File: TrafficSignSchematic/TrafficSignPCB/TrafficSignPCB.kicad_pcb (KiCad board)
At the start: 2 copper layers, 106.7 x 78.7 mm, 27 parts, among them J1 IDC connector, J2 3.96mm pitch 4-pin polarized 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, J3 Power In, U1 ATmega328P-PU, U2 SIM800L, Y1 16MHz

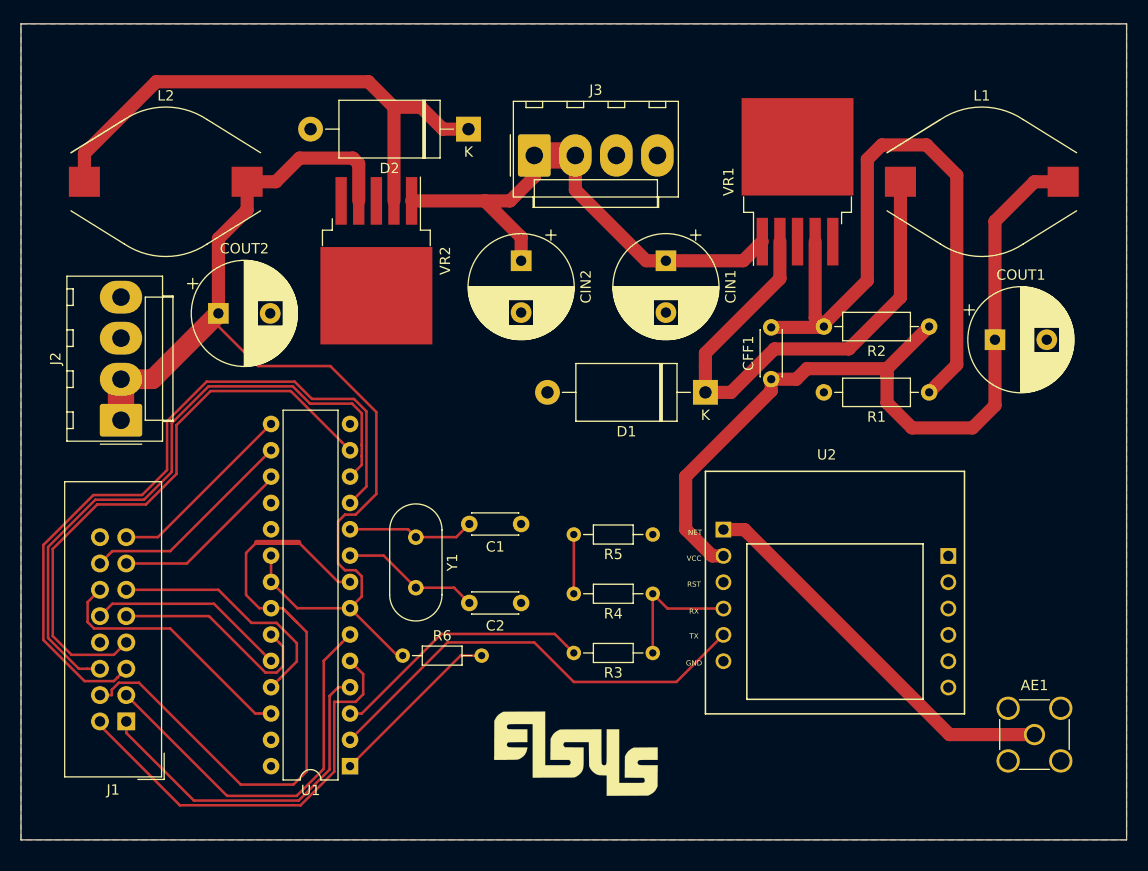
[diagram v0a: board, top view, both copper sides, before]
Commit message: Changed element placement and rerouted board
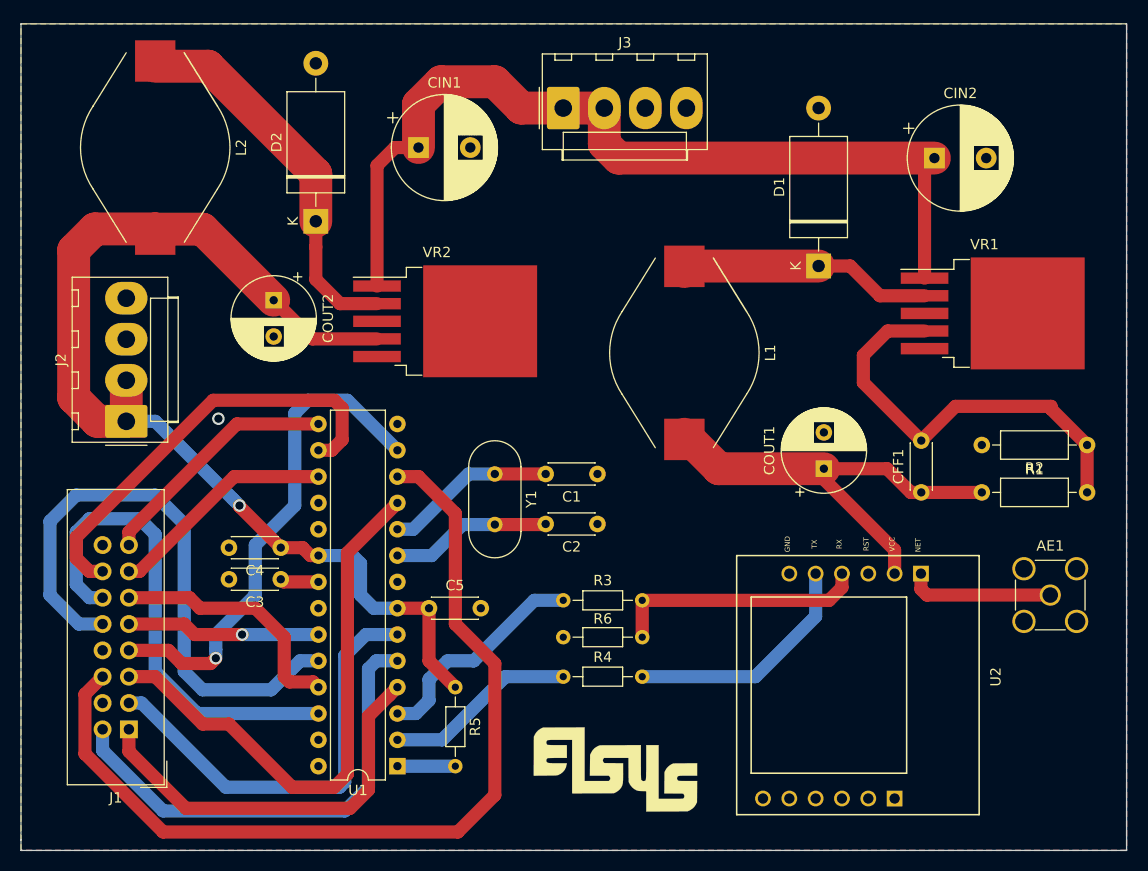
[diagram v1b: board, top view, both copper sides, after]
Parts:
- added C3: 100n, Capacitor_THT:C_Disc_D4.3mm_W1.9mm_P5.00mm, F.Cu at (72.1, 119.6)
- added C4: 100n, Capacitor_THT:C_Disc_D4.3mm_W1.9mm_P5.00mm, F.Cu at (72.1, 116.6)
- added C5: 100n, Capacitor_THT:C_Disc_D4.3mm_W1.9mm_P5.00mm, F.Cu at (86.4, 122.4)
- COUT1, COUT2: footprint Capacitor_THT:CP_Radial_D10.0mm_P5.00mm -> Capacitor_THT:CP_Radial_D8.0mm_P3.50mm
- R4: value 10k -> 20k
- moved CIN2 41.1 mm to (135.1, 79.0), turned to 0 degrees
- moved L1 33.1 mm to (111.0, 97.8), turned to 270 degrees
- moved U2 27.6 mm to (139.4, 117.3), turned to 270 degrees
- moved CIN1 26.3 mm to (85.3, 78.0), turned to 0 degrees
- moved VR1 22.1 mm to (140.0, 94.0), turned to 0 degrees
- moved COUT1 20.7 mm to (124.5, 109.0), turned to 90 degrees
- moved R5 18.6 mm to (88.9, 130.0), turned to 270 degrees
- moved CFF1 18.1 mm to (133.9, 111.3)
- moved D2 17.2 mm to (75.4, 85.1), turned to 90 degrees
- moved R2 16.8 mm to (139.7, 111.3), turned to 0 degrees
- moved D1 16.4 mm to (124.0, 89.4), turned to 90 degrees
- moved R1 16.1 mm to (149.9, 106.7)
- moved R6 15.6 mm to (99.3, 129.0)
- moved AE1 13.5 mm to (146.3, 121.2)
- moved C2 10.6 mm to (102.6, 114.3)
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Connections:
- R4 pad 2: Net-(R4-Pad2) -> GND
- R5 pad 1: Net-(R4-Pad2) -> +5V
- R5 pad 2: GND -> Net-(R5-Pad2)
- R6 pad 1: +5V -> /RXD
- U1 pad 1: Net-(R6-Pad2) -> Net-(R5-Pad2)
- U1 pad 21: +5V -> Net-(C3-Pad1)
- U2 pad 5: /RXD -> Net-(R6-Pad2)
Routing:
- net GND: track 64.2 -> 0.00 mm, vias 0 -> 1
- net B: track 19.3 -> 57.6 mm
- net +4V: track 81.5 -> 44.0 mm
- net +12V: track 51.0 -> 88.3 mm
- net Net-(D1-Pad1): track 51.3 -> 24.6 mm
- net G1: track 62.1 -> 88.1 mm
- net /RXD: track 43.4 -> 18.5 mm
- net Net-(AE1-Pad1): track 38.2 -> 14.2 mm
- net Net-(CFF1-Pad2): track 64.0 -> 41.1 mm
- net D: track 25.0 -> 47.6 mm
- net STB: track 21.0 -> 42.3 mm
- net Net-(D2-Pad1): track 53.6 -> 36.9 mm
- net R1: track 70.4 -> 54.2 mm
- net Net-(R3-Pad2): track 13.1 -> 24.7 mm
- net B1: track 56.9 -> 48.3 mm, vias 0 -> 1
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- added copper zone on B.Cu, net GND
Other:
- board size 106.7 x 78.7 mm -> 106.7 x 79.8 mm
- rule via_min_size: 0.4 -> 0.5

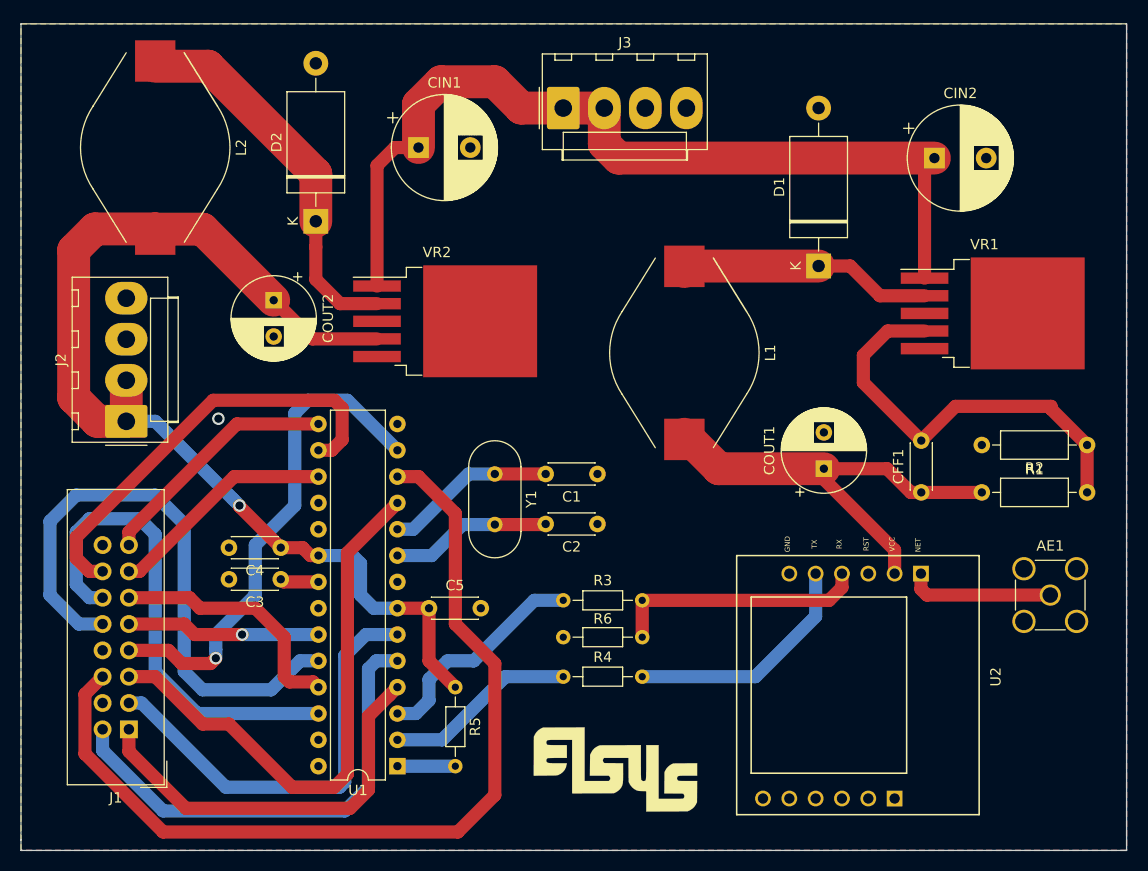
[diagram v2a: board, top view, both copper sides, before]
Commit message: Changed buck converter layout
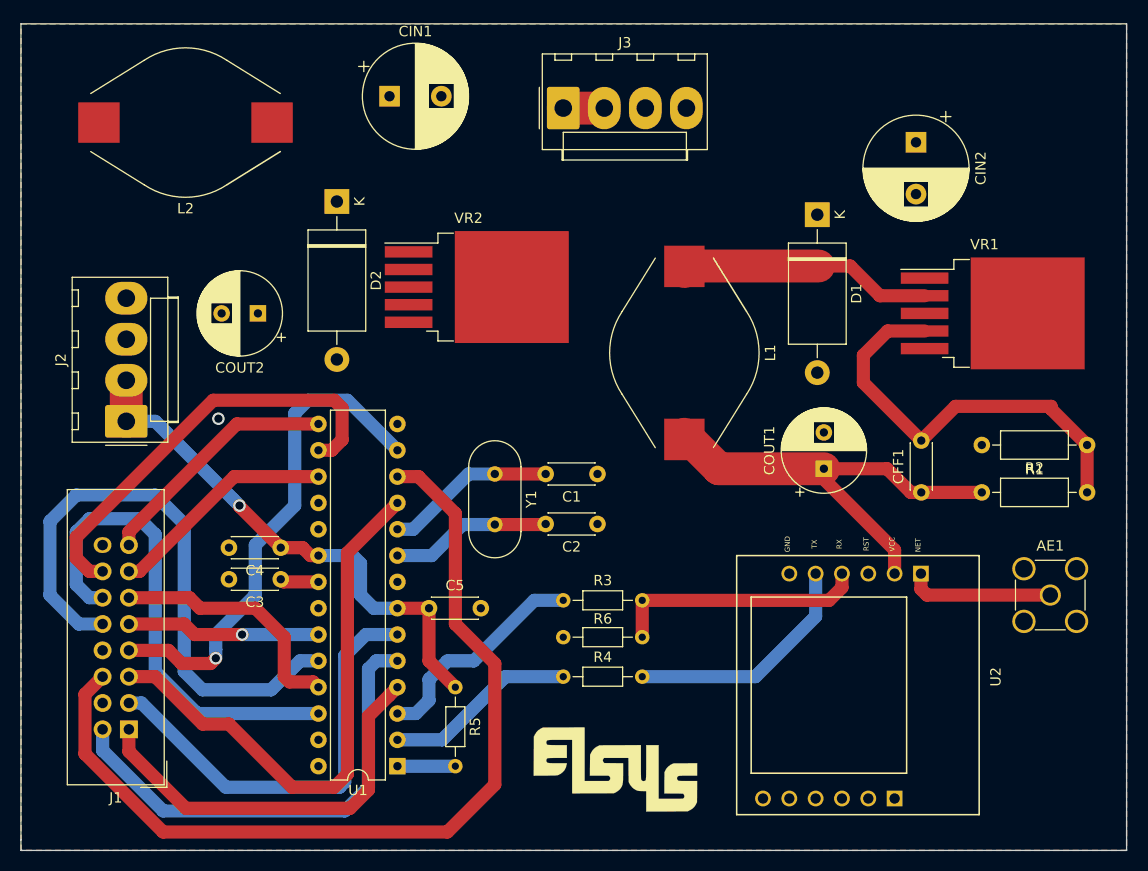
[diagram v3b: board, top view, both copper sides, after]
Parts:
- moved CIN1 5.69 mm to (82.5, 73.0)
- moved D1 4.95 mm to (123.8, 84.5), turned to 270 degrees
- moved VR2 4.49 mm to (90.2, 91.4)
- moved L2 3.79 mm to (62.9, 75.6), turned to 180 degrees
- moved D2 2.79 mm to (77.5, 83.2), turned to 270 degrees
- moved CIN2 2.34 mm to (133.3, 77.5), turned to 270 degrees
- moved COUT2 1.98 mm to (69.8, 94.0), turned to 180 degrees
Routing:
- net +12V: track 88.3 -> 3.96 mm
- net +5V: track 105.9 -> 51.1 mm
- net Net-(D2-Pad1): track 36.9 -> 0.00 mm
- net G1: track 88.1 -> 87.5 mm
